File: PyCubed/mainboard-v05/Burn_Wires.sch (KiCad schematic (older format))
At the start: 22 parts, among them Q20 NDS8434, Q21 NDS8434, Q4 IRLML2803, Q5 IRLML2803, Q6 MMBT2222AT, U16 PE014006

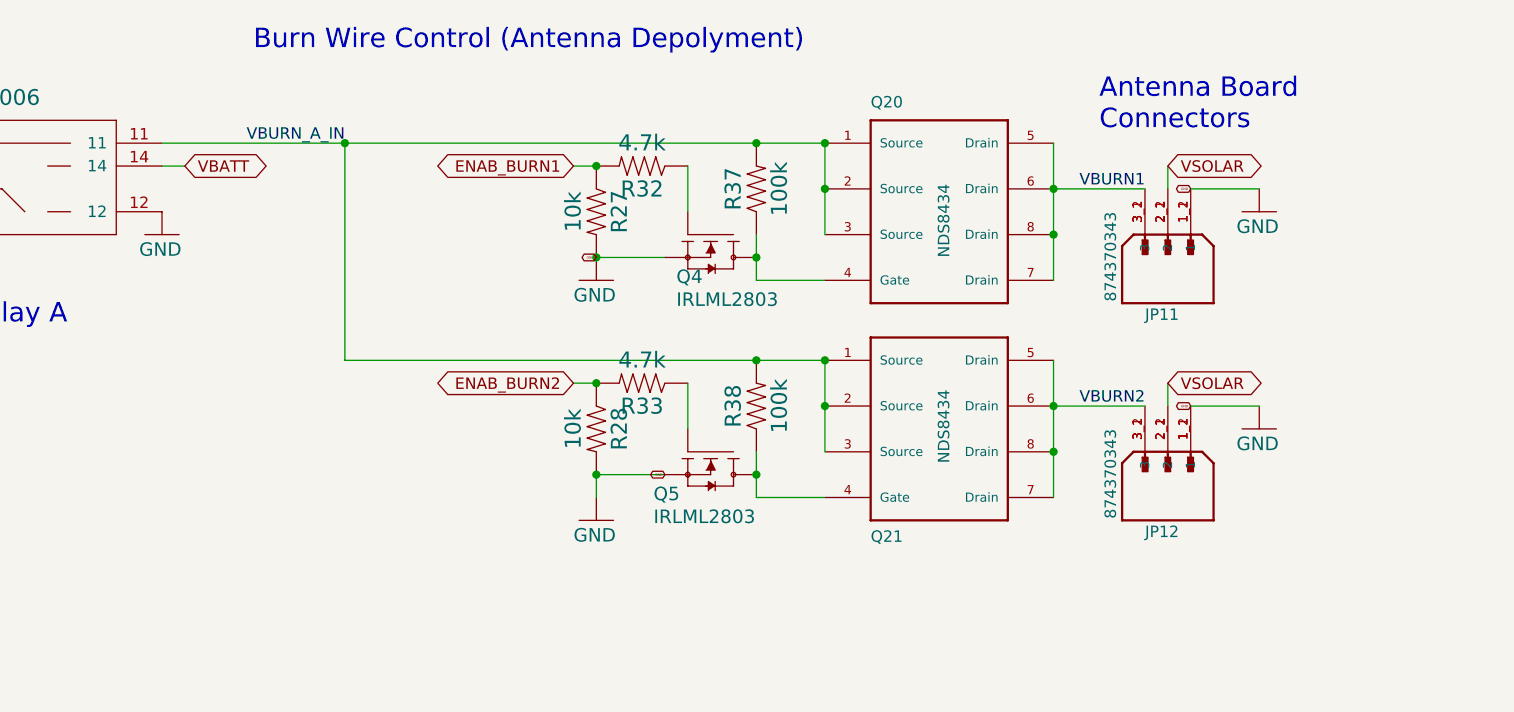
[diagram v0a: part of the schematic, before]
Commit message: radio and gps moved to make space for limit switches
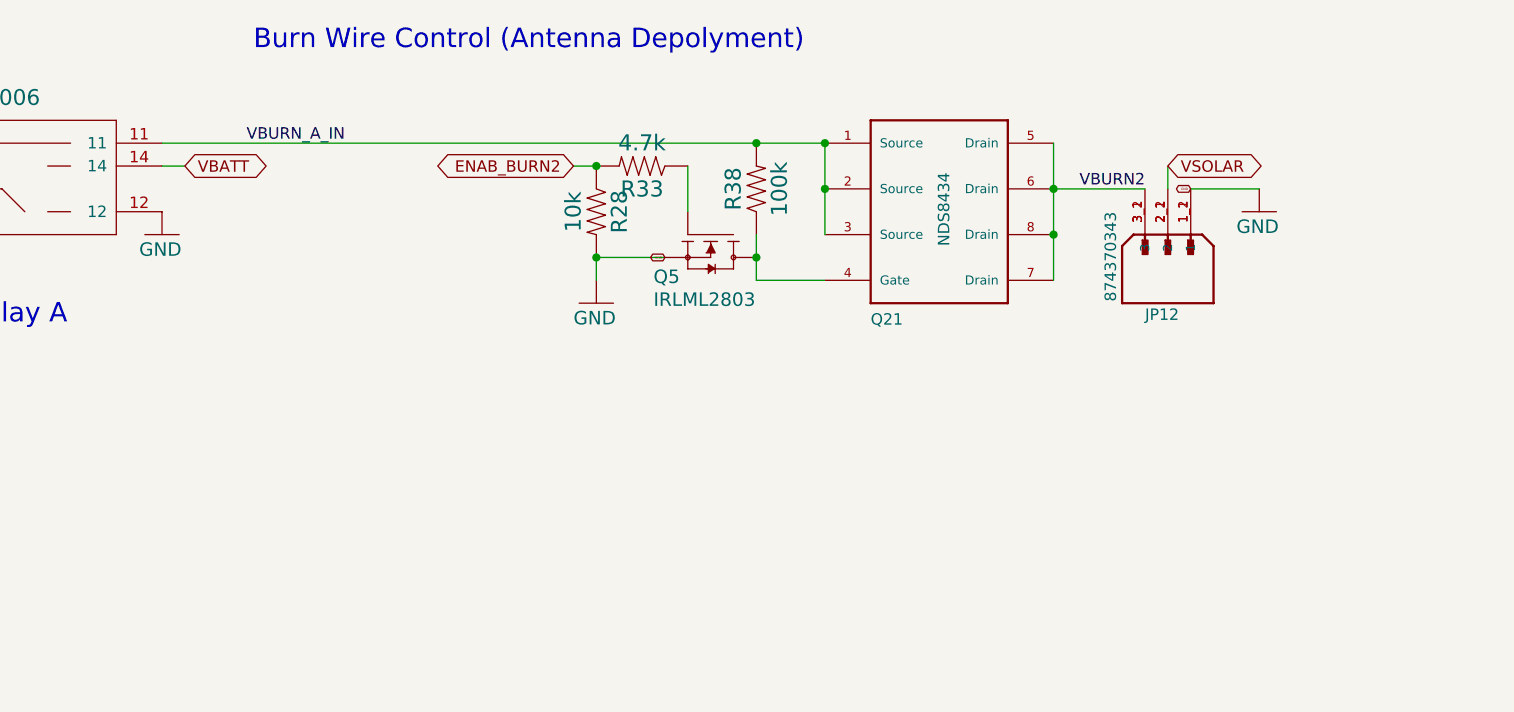
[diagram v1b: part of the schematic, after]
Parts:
- removed JP11: 874370343, mainboard:MOLEX_874370343, symbol mainboard:874370343
- removed Q20: NDS8434, mainboard:NDS8434, symbol mainboard:NDS8434
- removed Q4: IRLML2803, mainboard:SOT-23, symbol mainboard:IRLML2803TRPBF
- removed R27: 10k, Resistor_SMD:R_0603_1608Metric, symbol mainboard:RESISTOR0603
- removed R32: 4.7k, Resistor_SMD:R_0603_1608Metric, symbol mainboard:RESISTOR0603
- removed R37: 100k, Resistor_SMD:R_0603_1608Metric, symbol mainboard:RESISTOR0603
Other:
- note removed: "Antenna Board\nConnectors"
- moved on the sheet: JP12, Q21, Q5, R28, R33, R38

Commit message: pycubed finished, awaiting review
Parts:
- removed JP10, JP13, JP14, JP15, JP8, JP9: MOLEX_Sherlock_2pos, mainboard:MOLEX_Sherlock_2pos, symbol mainboard:MOLEX_Sherlock_2pos
- removed JP12: 874370343, mainboard:MOLEX_874370343, symbol mainboard:874370343
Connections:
- net ENAB_BURN2 renamed ENAB_BURN
- net VBURN2 renamed BURN
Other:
- note removed: "Solar Panel Connectors"
